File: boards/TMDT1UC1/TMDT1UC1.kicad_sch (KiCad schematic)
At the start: 51 parts, among them J1 TC2050, U1 DW3210, U2 STM32U575RGTx, U3 LIS2DH, U4 TPS61222DCK-FIXED, Y1 ABM8-38.400MHZ-12-D1G-T

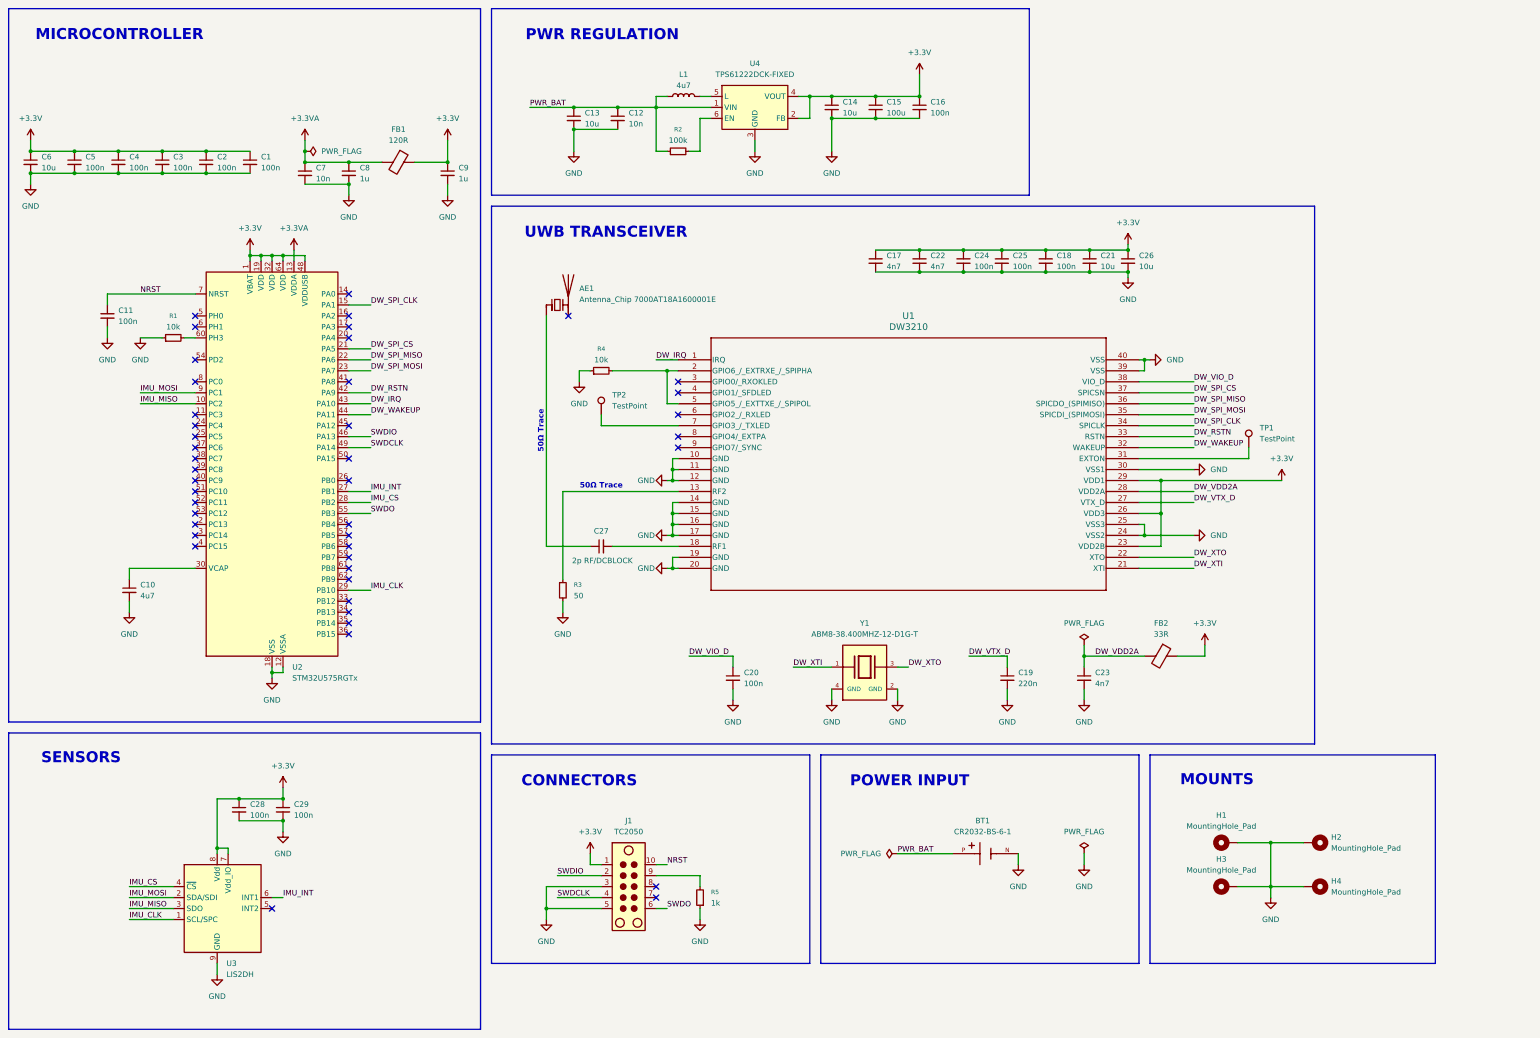
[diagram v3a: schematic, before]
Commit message: Started switching chips to simpler design on tag (needed factory calibration for reliable TWR)
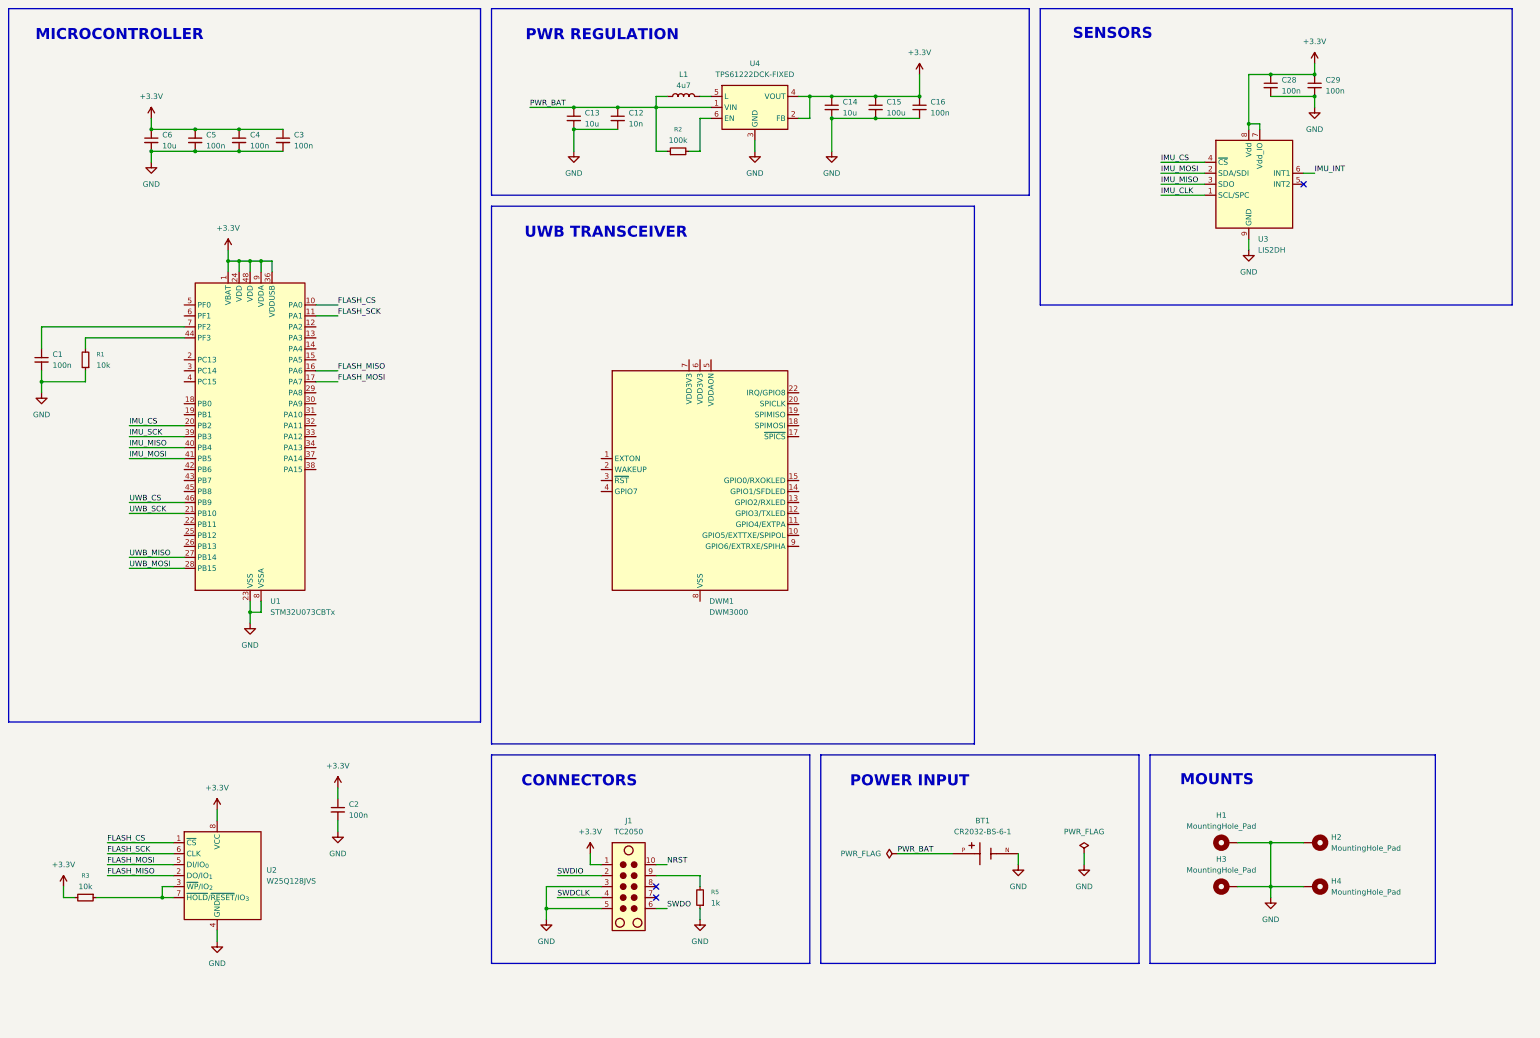
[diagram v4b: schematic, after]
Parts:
- removed AE1: Antenna_Chip 7000AT18A1600001E, RF_Antenna:Johanson_2450AT18x100, symbol Device:Antenna_Chip
- removed C10: 4u7, Capacitor_SMD:C_0603_1608Metric, symbol Device:C_Small
- removed C11, C20: 100n, Capacitor_SMD:C_0402_1005Metric, symbol Device:C_Small
- removed C17, C22, C23: 4n7, Capacitor_SMD:C_0402_1005Metric, symbol Device:C_Small
- removed C18, C24, C25: 100n, Capacitor_SMD:C_0201_0603Metric, symbol Device:C_Small
- removed C19: 220n, Capacitor_SMD:C_0201_0603Metric, symbol Device:C_Small
- removed C21, C26: 10u, Capacitor_SMD:C_0603_1608Metric, symbol Device:C_Small
- removed C27: 2p RF/DCBLOCK, Capacitor_SMD:C_0402_1005Metric, symbol Device:C_Small
- removed C7: 10n, Capacitor_SMD:C_0402_1005Metric, symbol Device:C_Small
- removed C8, C9: 1u, Capacitor_SMD:C_0603_1608Metric, symbol Device:C_Small
- removed FB1: 120R, Inductor_SMD:L_0603_1608Metric, symbol Device:FerriteBead
- removed FB2: 33R, Inductor_SMD:L_0603_1608Metric, symbol Device:FerriteBead
- removed R4: 10k, Resistor_SMD:R_0402_1005Metric, symbol Device:R_Small
- removed TP1, TP2: TestPoint, TestPoint:TestPoint_Pad_D1.0mm, symbol Connector:TestPoint
- removed U1: DW3210, meridian:qfn_DW3210_QOR, symbol dw3210:DW3210
- removed U2: STM32U575RGTx, Package_QFP:LQFP-64_10x10mm_P0.5mm, symbol MCU_ST_STM32U5:STM32U575RGTx
- removed Y1: ABM8-38.400MHZ-12-D1G-T, meridian:XTAL_ABM8-38.400MHZ-12-D1G-T, symbol ABM8-38.400MHZ-12-D1G-T:ABM8-38.400MHZ-12-D1G-T
- added DWM1: DWM3000, RF_Module:DWM1000, symbol RF_Module:DWM3000
- added U1: STM32U073CBTx, Package_QFP:LQFP-48_7x7mm_P0.5mm, symbol MCU_ST_STM32U0:STM32U073CBTx
- added U2: W25Q128JVS, Package_SO:SOIC-8_5.3x5.3mm_P1.27mm, symbol Memory_Flash:W25Q128JVS
- R1: footprint Resistor_SMD:R_0402_1005Metric -> (none)
- R3: value 50 -> 10k; footprint Resistor_SMD:R_0402_1005Metric -> (none)
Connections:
- net +3.3V: now also R3.2, U1.1 (VBAT), U1.24 (VDD), U1.36 (VDDUSB), U1.48 (VDD), U1.9 (VDDA), U2.8 (VCC); no longer C1.1
- net GND: now also U1.23 (VSS), U1.35 (VSS), U1.47 (VSS), U1.8 (VSSA), U2.4 (GND); no longer R3.2
- net IMU_CS: now also U1.20 (PB2)
- net IMU_MISO: now also U1.40 (PB4)
- net IMU_MOSI: now also U1.41 (PB5)
- net at R3.1: now also U2.3 (~{WP}/IO_{2}), U2.7 (~{HOLD}/~{RESET}/IO_{3})
- net at R1.2: now also U1.44 (PF3)
- new net: DWM1.16 (VSS), DWM1.21 (VSS), DWM1.23 (VSS), DWM1.24 (VSS), DWM1.8 (VSS)
- new net: C1.1, U1.7 (PF2)
- new net FLASH_CS: U1.10 (PA0), U2.1 (~{CS})
- new net FLASH_MISO: U1.16 (PA6), U2.2 (DO/IO_{1})
- new net FLASH_MOSI: U1.17 (PA7), U2.5 (DI/IO_{0})
- new net FLASH_SCK: U1.11 (PA1), U2.6 (CLK)
- new net IMU_SCK: U1.39 (PB3)
- new net UWB_CS: U1.46 (PB9)
- new net UWB_MISO: U1.27 (PB14)
- new net UWB_MOSI: U1.28 (PB15)
- new net UWB_SCK: U1.21 (PB10)
- no-connect marks 44 -> 3
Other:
- note removed: "50Ω Trace"
- moved on the sheet: C28, C29, C3, C4, C5, C6, U3

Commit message: Updated PCB (testing auto router)
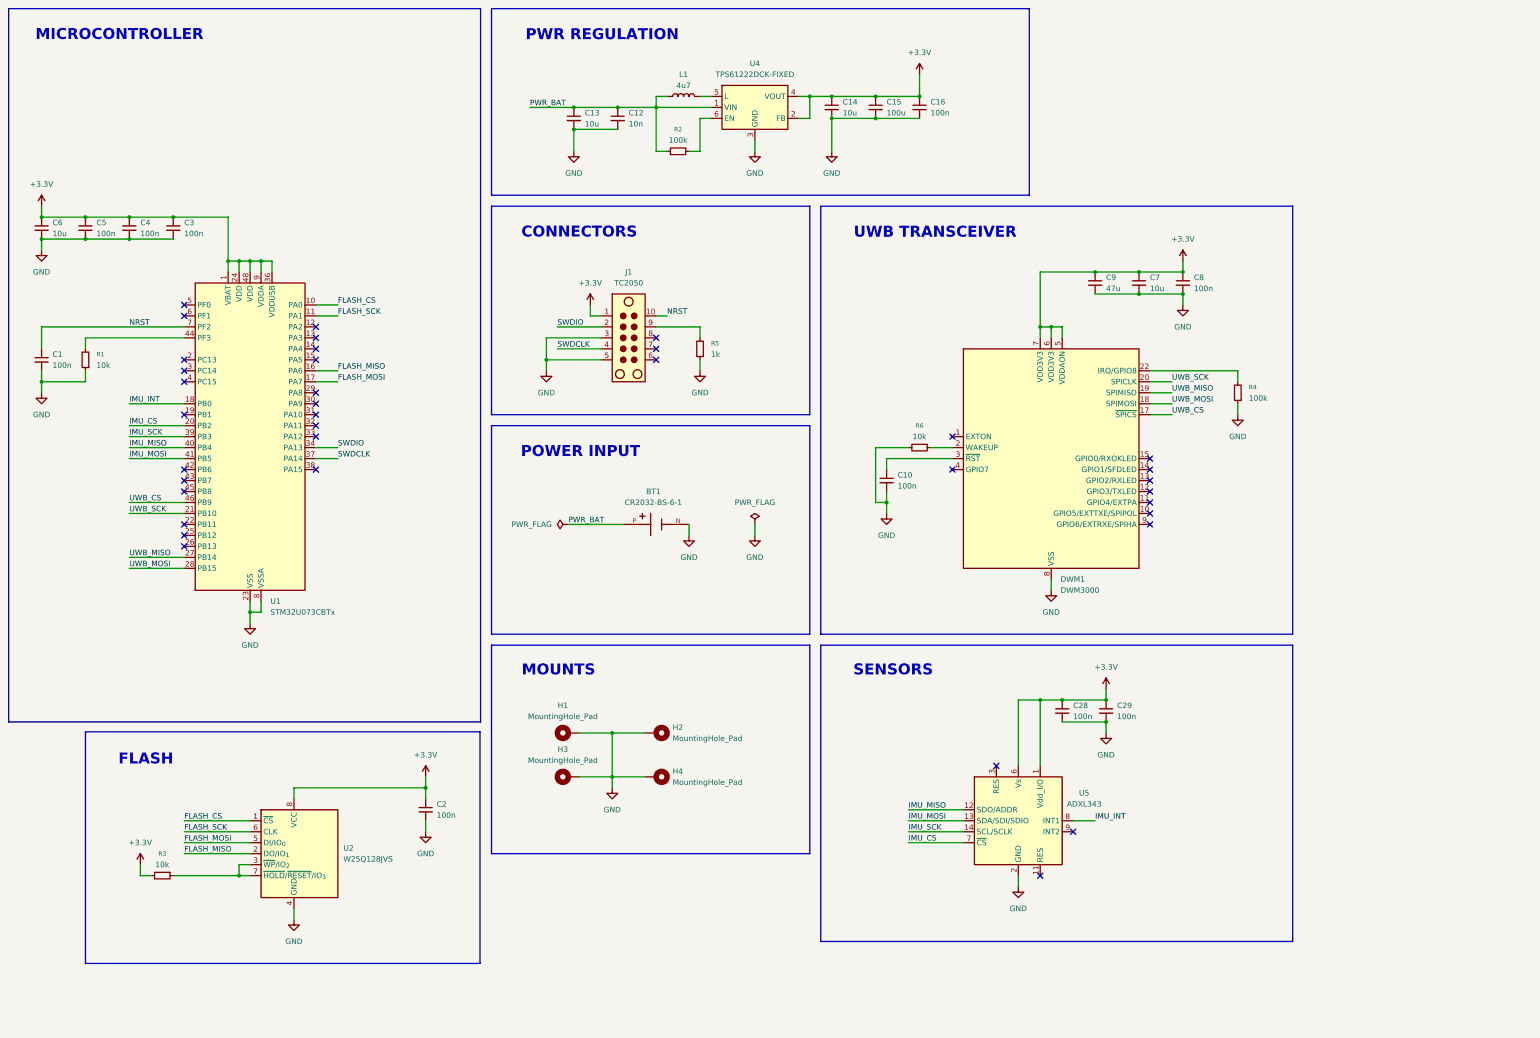
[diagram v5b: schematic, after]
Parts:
- removed U3: LIS2DH, Package_LGA:LGA-14_2x2mm_P0.35mm_LayoutBorder3x4y, symbol Sensor_Motion:LIS2DH
- added C10, C8: 100n, Capacitor_SMD:C_0402_1005Metric, symbol Device:C_Small
- added C7: 10u, Capacitor_SMD:C_0603_1608Metric, symbol Device:C_Small
- added C9: 47u, Capacitor_SMD:C_0603_1608Metric, symbol Device:C_Small
- added R4: 100k, Resistor_SMD:R_0402_1005Metric, symbol Device:R_Small
- added R6: 10k, Resistor_SMD:R_0402_1005Metric, symbol Device:R_Small
- added U5: ADXL343, Package_LGA:LGA-14_3x5mm_P0.8mm_LayoutBorder1x6y, symbol Sensor_Motion:ADXL343
- C13, C14, C6: footprint Capacitor_SMD:C_0402_1005Metric -> Capacitor_SMD:C_0603_1608Metric
- R1, R3: footprint (none) -> Resistor_SMD:R_0402_1005Metric
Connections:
- net +3.3V: now also DWM1.5 (VDDAON), DWM1.6 (VDD3V3), DWM1.7 (VDD3V3), C7.1, C8.1, C9.1, U5.1 (Vdd_I/O), U5.6 (Vs)
- net GND: now also DWM1.16 (VSS), DWM1.21 (VSS), DWM1.23 (VSS), DWM1.24 (VSS), DWM1.8 (VSS), C10.2, C7.2, C8.2, C9.2, R4.1, R6.2, U5.2 (GND), U5.4 (GND), U5.5 (GND)
- net IMU_CS: now also U5.7 (~{CS})
- net IMU_INT: now also U1.18 (PB0), U5.8 (INT1)
- net IMU_MISO: now also U5.12 (SDO/ADDR)
- net IMU_MOSI: now also U5.13 (SDA/SDI/SDIO)
- net IMU_SCK: now also U5.14 (SCL/SCLK)
- net NRST: now also C1.1, U1.7 (PF2)
- net SWDCLK: now also U1.37 (PA14)
- net SWDIO: now also U1.34 (PA13)
- net UWB_CS: now also DWM1.17 (~{SPICS})
- net UWB_MISO: now also DWM1.19 (SPIMISO)
- net UWB_MOSI: now also DWM1.18 (SPIMOSI)
- net UWB_SCK: now also DWM1.20 (SPICLK)
- net at DWM1.2 (WAKEUP): now also R6.1
- net at DWM1.22 (IRQ/GPIO8): now also R4.2
- net at DWM1.3 (~{RST}): now also C10.1
- net SWDO: no longer names the net of J1.6
- no-connect marks 3 -> 37
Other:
- note added: "FLASH"
- moved on the sheet: BT1, C2, C28, C29, C3, C4, C5, C6, DWM1, H1, H2, H3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

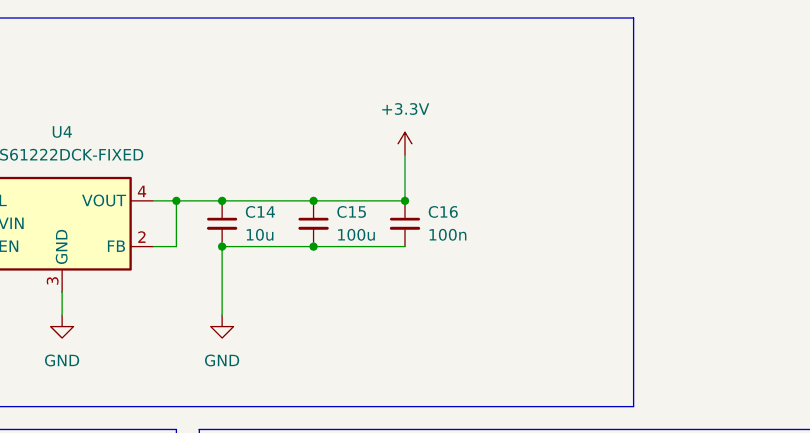
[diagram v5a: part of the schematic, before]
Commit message: Updated board (switched to 4 layer, rerouted cleaner)
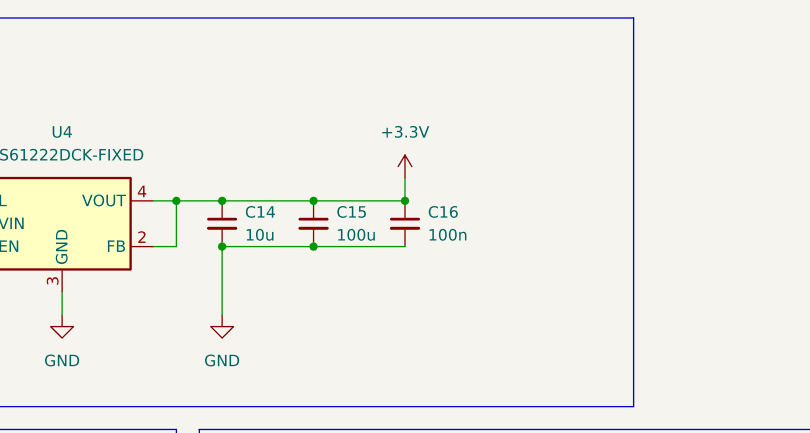
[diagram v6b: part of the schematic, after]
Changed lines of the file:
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@@
 	)
 	(junction
-		(at 142.24 99.06)
+		(at 228.6 38.1)
 		(diameter 0)
 		(color 0 0 0 0)
 	)
 	(junction
-		(at 148.59 40.64)
+		(at 142.24 99.06)
 		(diameter 0)
 		(color 0 0 0 0)
 	)
 	(junction
-		(at 25.4 104.14)
+		(at 148.59 40.64)
 		(diameter 0)
 		(color 0 0 0 0)
 	)
 	(junction
-		(at 228.6 38.1)
+		(at 25.4 104.14)
 		(diameter 0)
 		(color 0 0 0 0)
@@
 	(wire
 		(pts
-			(xy 228.6 33.02) (xy 228.6 38.1)
+			(xy 264.16 205.74) (xy 269.24 205.74)
 		)
 		(stroke
@@
 	(wire
 		(pts
-			(xy 264.16 205.74) (xy 269.24 205.74)
+			(xy 144.78 96.52) (xy 154.94 96.52)
 		)
 		(stroke
@@
 	(wire
 		(pts
-			(xy 144.78 96.52) (xy 154.94 96.52)
+			(xy 71.12 215.9) (xy 71.12 218.44)
 		)
 		(stroke
@@
 	(wire
 		(pts
-			(xy 71.12 215.9) (xy 71.12 218.44)
+			(xy 228.6 35.56) (xy 228.6 38.1)
 		)
 		(stroke
@@
 	)
 	(symbol
+		(lib_id "power:+3.3V")
+		(at 228.6 35.56 0)
+		(unit 1)
+		(exclude_from_sim no)
+		(in_bom yes)
+		(on_board yes)
+		(dnp no)
+		(fields_autoplaced yes)
+		(property "Reference" "#PWR012"
+			(at 228.6 39.37 0)
+			(effects
+				(font
+					(size 1.27 1.27)
+				)
+				(hide yes)
+			)
+		)
+		(property "Value" "+3.3V"
+			(at 228.6 30.48 0)
+			(effects
+				(font
+					(size 1.27 1.27)
+				)
+			)
+		)
+		(property "Footprint" ""
+			(at 228.6 35.56 0)
+			(effects
+				(font
+					(size 1.27 1.27)
+				)
+				(hide yes)
+			)
+		)
+		(property "Datasheet" ""
+			(at 228.6 35.56 0)
+			(effects
+				(font
+					(size 1.27 1.27)
+				)
+				(hide yes)
+			)
+		)
+		(property "Description" "Power symbol creates a global label with name \"+3.3V\""
+			(at 228.6 35.56 0)
+			(effects
+				(font
+					(size 1.27 1.27)
+				)
+				(hide yes)
+			)
+		)
+		(pin "1"
+		)
+		(instances
+			(project "TMDT1UC1"
+				(path "/7e70e283-abbb-484b-a110-f07ee4f07f76"
+					(reference "#PWR012")
+					(unit 1)
+				)
+			)
+		)
+	)
+	(symbol
 		(lib_id "power:GND")
 		(at 271.78 185.42 0)
@@
 					(unit 1)
 				)
-			)
-		)
-	)
-	(symbol
-		(lib_id "power:+3.3V")
-		(at 228.6 33.02 0)
-		(unit 1)
-		(exclude_from_sim no)
-		(in_bom yes)
-		(on_board yes)
-		(dnp no)
-		(fields_autoplaced yes)
-		(property "Reference" "#PWR018"
-			(at 228.6 36.83 0)
-			(effects
-				(font
-					(size 1.27 1.27)
-				)
-				(hide yes)
-			)
-		)
-		(property "Value" "+3.3V"
-			(at 228.6 27.94 0)
-			(effects
-				(font
-					(size 1.27 1.27)
-				)
-			)
-		)
-		(property "Footprint" ""
-			(at 228.6 33.02 0)
-			(effects
-				(font
-					(size 1.27 1.27)
-				)
-				(hide yes)
-			)
-		)
-		(property "Datasheet" ""
-			(at 228.6 33.02 0)
-			(effects
-				(font
-					(size 1.27 1.27)
-				)
-				(hide yes)
-			)
-		)
-		(property "Description" "Power symbol creates a global label with name \"+3.3V\""
-			(at 228.6 33.02 0)
-			(effects
-				(font
-					(size 1.27 1.27)
-				)
-				(hide yes)
-			)
-		)
-		(pin "1"
-		)
-		(instances
-			(project "TMDT1UC1"
-				(path "/7e70e283-abbb-484b-a110-f07ee4f07f76"
-					(reference "#PWR018")
-					(unit 1)
-				)
